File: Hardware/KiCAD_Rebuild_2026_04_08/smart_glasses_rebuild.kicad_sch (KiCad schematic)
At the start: 10 parts, among them U1 ESP32-WROVER-dev

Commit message: kicad manual checkpoint
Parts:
- removed J?: OV2640_CONN, symbol custom_symbols:OV2640_Connector_24Pin_Signal
- removed LS? (x2): Small Speaker, symbol custom_symbols:Speaker_Small_2Pin
- removed U1, U?: ESP32-WROVER-dev, symbol custom_symbols:ESP32-WROVER-dev
- removed U?: HW-104, symbol custom_symbols:HW-104_Amplifier_Module_9P
- removed U?: HW-104, symbol custom_symbols:HW-104_Amplifier_Module
- removed U?: INMP441, symbol custom_symbols:INMP441_Mic_Module
- removed U?: HW-763, symbol custom_symbols:HW-763_Touch_Module
- removed U?: OV2640, symbol custom_symbols:OV2640_Camera_Module_24P_Signal
- added LS1, LS2: Small Speaker, Connector_PinHeader_2.54mm:PinHeader_1x02_P2.54mm_Vertical, symbol custom_symbols:Speaker_Small_2Pin
- added S1: TP4056_BMS, Connector_PinHeader_2.54mm:PinHeader_1x06_P2.54mm_Vertical, symbol custom_symbols:TP4056_BMS_Module
- added U1: HW-104, Connector_PinHeader_2.54mm:PinHeader_1x09_P2.54mm_Vertical, symbol custom_symbols:HW-104_Amplifier_Module_9P
- added U2: MPU-6050_Breakout, Connector_PinHeader_2.54mm:PinHeader_1x08_P2.54mm_Vertical, symbol custom_symbols:MPU6050_Breakout_8P
- added U3: INMP441, Connector_PinHeader_2.54mm:PinHeader_1x06_P2.54mm_Vertical, symbol custom_symbols:INMP441_Mic_Module
- added U4: IIC_OLED, Connector_PinHeader_2.54mm:PinHeader_1x04_P2.54mm_Vertical, symbol custom_symbols:IIC_OLED_Module
- added U5: HW-763, Connector_PinHeader_2.54mm:PinHeader_1x03_P2.54mm_Vertical, symbol custom_symbols:HW-763_Touch_Module
- added U7: ESP32-WROVER-dev, RebuildLib:ESP32_WROVER_DEV_2x19_WIDE, symbol custom_symbols:ESP32-WROVER-dev
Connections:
- new net: U1.1 (VCC), U2.1 (VCC), U3.1 (VDD), U4.1 (VCC), U5.1 (VCC), U7.1 (3V3)
- new net: U1.2 (GND), U1.5 (SIG_GND), U2.2 (GND), U3.2 (GND), U4.2 (GND), U5.2 (GND), U7.20 (GND)
- new net: U1.3 (LIN), U7.9 (GPIO25)
- new net: U1.4 (RIN), U7.10 (GPIO26)
- new net: LS2.1 (+), U1.6 (L+)
- new net: LS2.2 (-), U1.7 (L-)
- new net: LS1.1 (+), U1.8 (R+)
- new net: LS1.2 (-), U1.9 (R-)
- new net: U2.3 (SCL), U4.3 (SCL), U7.22 (GPIO22)
- new net: U2.4 (SDA), U4.4 (SDA), U7.25 (GPIO21)
- new net: U5.3 (SIG), U7.15 (GPIO13)
- new net: U3.3 (SCK), U7.12 (GPIO14)
- new net: S1.6 (OUT-), U7.14 (GND)
- new net: S1.5 (OUT+), U7.19 (5V)
- new net: U3.6 (L/R), U7.26 (GND)
- new net: U3.5 (SD), U7.32 (GPIO4)
- new net: U3.4 (WS), U7.35 (GPIO15)
- new net +3.3V: S1.3 (B+)
- new net GND: S1.4 (B-)
- no-connect marks 0 -> 27

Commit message: kicad almost done
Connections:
- net at U1.1 (GND), U3.1 (GND), U4.1 (GND)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: now also U1.4 (SIG_GND), U2.2 (GND), U7.20 (GND); no longer U2.1 (VCC), U7.1 (3V3)
- net at U1.3 (RIN): now also U7.10 (GPIO26); no longer U7.9 (GPIO25)
- net at U7.15 (GPIO13): now also U5.2 (SIG); no longer U5.3 (SIG)
- net at U7.12 (GPIO14): now also U3.4 (SCK); no longer U3.3 (SCK)
- net at U7.32 (GPIO4): now also U3.3 (SD); no longer U3.5 (SD)
- net at U7.35 (GPIO15): now also U3.5 (WS); no longer U3.4 (WS)
- net +3.3V: no longer names the net of S1.3 (B+)
- net GND: no longer names the net of S1.4 (B-)
- new net: U1.2 (VCC), U2.1 (VCC), U3.2 (VDD), U4.2 (VCC), U5.1 (GND), U7.1 (3V3)
- new net: U1.5 (LIN), U7.9 (GPIO25)
- no-connect marks 27 -> 29
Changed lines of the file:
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@@
+	)
+	(no_connect
+		(at 34.29 96.52)
 	)
 	(no_connect
@@
 	(no_connect
 		(at 80.01 93.98)
+	)
+	(no_connect
+		(at 34.29 99.06)
 	)
 	(no_connect
@@
 	)
 	(symbol
-		(lib_id "power:GND")
-		(at 34.29 99.06 270)
-		(unit 1)
-		(exclude_from_sim no)
-		(in_bom yes)
-		(on_board yes)
-		(dnp no)
-		(fields_autoplaced yes)
-		(property "Reference" "#PWR02"
-			(at 27.94 99.06 0)
-			(effects
-				(font
-					(size 1.27 1.27)
-				)
-				(hide yes)
-			)
-		)
-		(property "Value" "GND"
-			(at 30.48 99.0599 90)
-			(effects
-				(font
-					(size 1.27 1.27)
-				)
-				(justify right)
-			)
-		)
-		(property "Footprint" ""
-			(at 34.29 99.06 0)
-			(effects
-				(font
-					(size 1.27 1.27)
-				)
-				(hide yes)
-			)
-		)
-		(property "Datasheet" ""
-			(at 34.29 99.06 0)
-			(effects
-				(font
-					(size 1.27 1.27)
-				)
-				(hide yes)
-			)
-		)
-		(property "Description" "Power symbol creates a global label with name \"GND\" , ground"
-			(at 34.29 99.06 0)
-			(effects
-				(font
-					(size 1.27 1.27)
-				)
-				(hide yes)
-			)
-		)
-		(pin "1"
-		)
-		(instances
-			(project "smart_glasses_rebuild"
-				(path "/dcee668c-9136-4a03-9e69-aac47204f643"
-					(reference "#PWR02")
-					(unit 1)
-				)
-			)
-		)
-	)
-	(symbol
 		(lib_id "custom_symbols:HW-763_Touch_Module")
 		(at 59.69 57.15 0)
@@
 			)
 		)
-		(pin "3"
+		(pin "1"
 		)
 		(pin "1"
@@
 					(unit 1)
 				)
-			)
-		)
-	)
-	(symbol
-		(lib_id "power:+3.3V")
-		(at 34.29 96.52 90)
-		(unit 1)
-		(exclude_from_sim no)
-		(in_bom yes)
-		(on_board yes)
-		(dnp no)
-		(fields_autoplaced yes)
-		(property "Reference" "#PWR01"
-			(at 38.1 96.52 0)
-			(effects
-				(font
-					(size 1.27 1.27)
-				)
-				(hide yes)
-			)
-		)
-		(property "Value" "+3.3V"
-			(at 30.48 96.5199 90)
-			(effects
-				(font
-					(size 1.27 1.27)
-				)
-				(justify left)
-			)
-		)
-		(property "Footprint" ""
-			(at 34.29 96.52 0)
-			(effects
-				(font
-					(size 1.27 1.27)
-				)
-				(hide yes)
-			)
-		)
-		(property "Datasheet" ""
-			(at 34.29 96.52 0)
-			(effects
-				(font
-					(size 1.27 1.27)
-				)
-				(hide yes)
-			)
-		)
-		(property "Description" "Power symbol creates a global label with name \"+3.3V\""
-			(at 34.29 96.52 0)
-			(effects
-				(font
-					(size 1.27 1.27)
-				)
-				(hide yes)
-			)
-		)
-		(pin "1"
-		)
-		(instances
-			(project "smart_glasses_rebuild"
-				(path "/dcee668c-9136-4a03-9e69-aac47204f643"
-					(reference "#PWR01")
-					(unit 1)
-				)

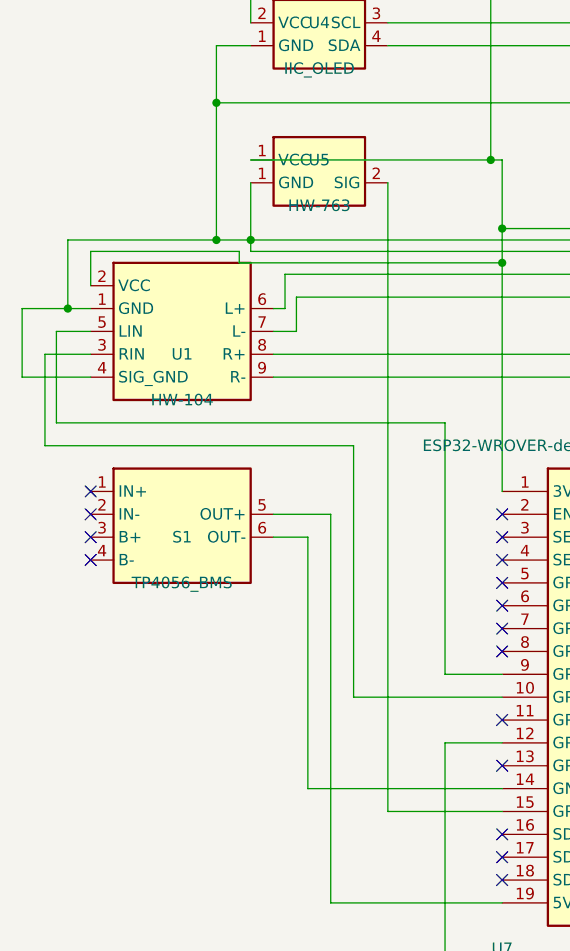
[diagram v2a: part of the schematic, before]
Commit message: kicad adding button for pwr
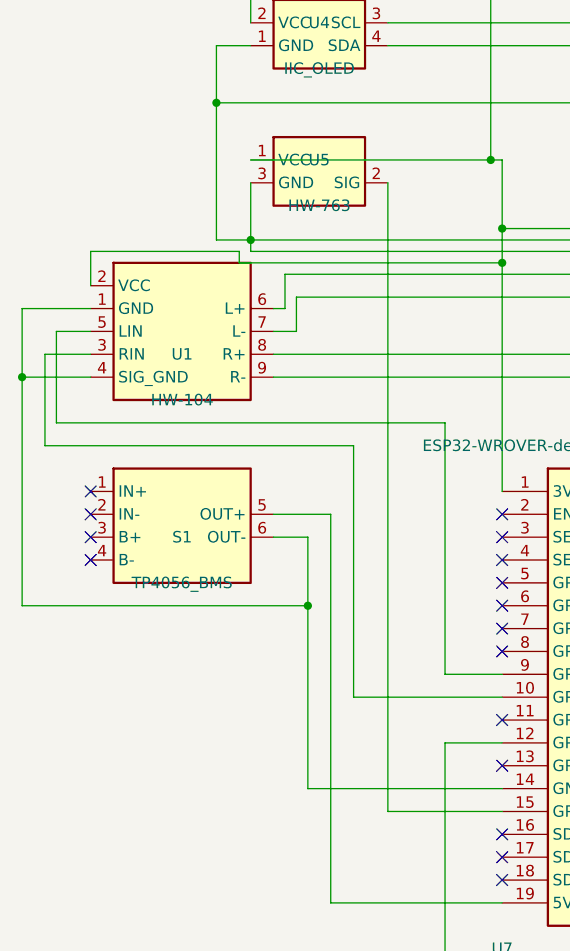
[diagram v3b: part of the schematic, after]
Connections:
- net at U2.2 (GND), U3.1 (GND), U4.1 (GND)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: now also U5.3 (GND); no longer U1.1 (GND), U1.4 (SIG_GND), U5.1 (GND)
- net at S1.6 (OUT-), U7.14 (GND): now also U1.1 (GND), U1.4 (SIG_GND)
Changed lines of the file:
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@@
 	(paper "A4")
-	(junction
-		(at 48.26 63.5)
-		(diameter 0)
-		(color 0 0 0 0)
-	)
 	(junction
 		(at 114.3 39.37)
@@
 	)
 	(junction
+		(at 58.42 104.14)
+		(diameter 0)
+		(color 0 0 0 0)
+	)
+	(junction
 		(at 52.07 63.5)
 		(diameter 0)
@@
 	)
 	(junction
-		(at 31.75 71.12)
-		(diameter 0)
-		(color 0 0 0 0)
-	)
-	(junction
 		(at 113.03 41.91)
 		(diameter 0)
@@
 		(color 0 0 0 0)
 	)
+	(junction
+		(at 26.67 78.74)
+		(diameter 0)
+		(color 0 0 0 0)
+	)
 	(no_connect
 		(at 110.49 93.98)
@@
 	(wire
 		(pts
+			(xy 26.67 71.12) (xy 26.67 78.74)
+		)
+		(stroke
+			(width 0)
+			(type default)
+		)
+	)
+	(wire
+		(pts
 			(xy 29.21 76.2) (xy 29.21 86.36)
 		)
@@
 	(wire
 		(pts
-			(xy 58.42 96.52) (xy 58.42 124.46)
+			(xy 58.42 96.52) (xy 58.42 104.14)
 		)
 		(stroke
@@
 	(wire
 		(pts
-			(xy 26.67 71.12) (xy 31.75 71.12)
-		)
-		(stroke
-			(width 0)
-			(type default)
-		)
-	)
-	(wire
-		(pts
 			(xy 144.78 129.54) (xy 144.78 63.5)
 		)
@@
 	(wire
 		(pts
-			(xy 31.75 63.5) (xy 48.26 63.5)
-		)
-		(stroke
-			(width 0)
-			(type default)
-		)
-	)
-	(wire
-		(pts
 			(xy 119.38 67.31) (xy 55.88 67.31)
 		)
@@
 	(wire
 		(pts
+			(xy 58.42 104.14) (xy 58.42 124.46)
+		)
+		(stroke
+			(width 0)
+			(type default)
+		)
+	)
+	(wire
+		(pts
 			(xy 119.38 78.74) (xy 54.61 78.74)
 		)
@@
 	(wire
 		(pts
-			(xy 34.29 71.12) (xy 31.75 71.12)
-		)
-		(stroke
-			(width 0)
-			(type default)
-		)
-	)
-	(wire
-		(pts
 			(xy 124.46 132.08) (xy 118.11 132.08)
 		)
@@
 	(wire
 		(pts
+			(xy 34.29 78.74) (xy 26.67 78.74)
+		)
+		(stroke
+			(width 0)
+			(type default)
+		)
+	)
+	(wire
+		(pts
 			(xy 30.48 83.82) (xy 30.48 73.66)
 		)
@@
 	(wire
 		(pts
-			(xy 26.67 78.74) (xy 26.67 71.12)
-		)
-		(stroke
-			(width 0)
-			(type default)
-		)
-	)
-	(wire
-		(pts
-			(xy 34.29 78.74) (xy 26.67 78.74)
-		)
-		(stroke
-			(width 0)
-			(type default)
-		)
-	)
-	(wire
-		(pts
 			(xy 29.21 86.36) (xy 63.5 86.36)
 		)
@@
 	(wire
 		(pts
+			(xy 34.29 71.12) (xy 26.67 71.12)
+		)
+		(stroke
+			(width 0)
+			(type default)
+		)
+	)
+	(wire
+		(pts
 			(xy 48.26 48.26) (xy 96.52 48.26)
 		)
@@
 	(wire
 		(pts
+			(xy 26.67 78.74) (xy 26.67 104.14)
+		)
+		(stroke
+			(width 0)
+			(type default)
+		)
+	)
+	(wire
+		(pts
 			(xy 114.3 39.37) (xy 67.31 39.37)
 		)
@@
 	(wire
 		(pts
+			(xy 26.67 104.14) (xy 58.42 104.14)
+		)
+		(stroke
+			(width 0)
+			(type default)
+		)
+	)
+	(wire
+		(pts
 			(xy 63.5 114.3) (xy 80.01 114.3)
 		)
@@
 		(pts
 			(xy 113.03 41.91) (xy 67.31 41.91)
-		)
-		(stroke
-			(width 0)
-			(type default)
-		)
-	)
-	(wire
-		(pts
-			(xy 31.75 71.12) (xy 31.75 63.5)
 		)
 		(stroke
@@
 		(pin "1"
 		)
-		(pin "1"
+		(pin "3"
 		)
 		(pin "2"

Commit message: Kicap Prototype 2 done
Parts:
- added SW1: PWR_SW_LATCH, RebuildLib:Power_Switch_Latching_SPST_2Pin, symbol custom_symbols:Power_Switch_Latching_SPST
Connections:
- net GND: now reaches S1.6 (OUT-), U1.1 (GND), U1.4 (SIG_GND), U7.14 (GND)
- net GND: now also U2.2 (GND), U3.1 (GND), U3.6 (L/R), U4.1 (GND), U5.3 (GND), U7.20 (GND), U7.26 (GND)
- net at U7.19 (5V): now also SW1.2; no longer S1.5 (OUT+)
- net SYS_PWR: now reaches S1.4 (B-)
- new net: S1.5 (OUT+), SW1.1
